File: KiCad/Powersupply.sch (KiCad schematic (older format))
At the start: 6 parts, among them J20 12V, U9 LM2596S-3.3

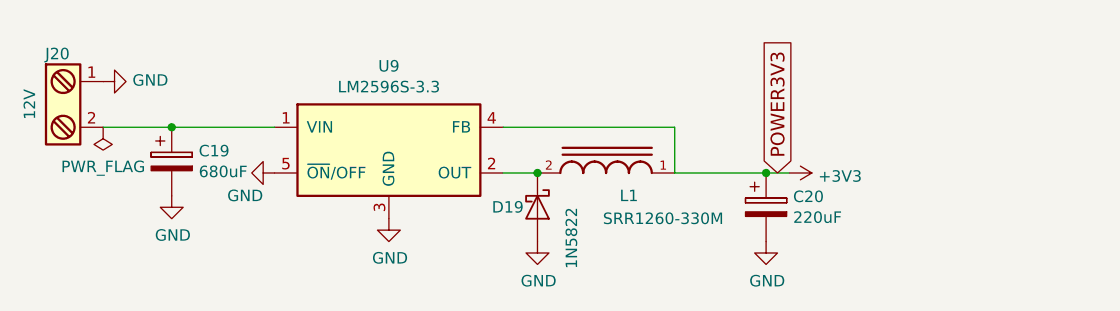
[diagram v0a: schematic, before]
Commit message: Use I2C for I/O
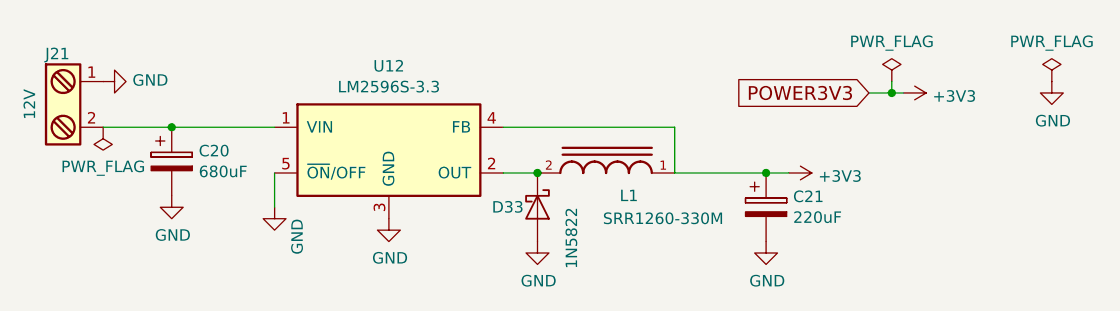
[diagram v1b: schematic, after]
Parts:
- L1: footprint INDP125125X600N -> SRR1260-330M:INDP125125X600N
- renumbered C19 to C20, C20 to C21, D19 to D33, J20 to J21, U9 to U12
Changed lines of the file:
@@
 LIBS:ESD_Protection
 LIBS:SRR1260-330M
+LIBS:ADS1115IDGST
 LIBS:HAP-IO-Card-cache
 EELAYER 26 0
@@
 $EndDescr
 $Comp
-L LM2596S-3.3 U9
+L LM2596S-3.3 U12
 U 1 1 591DBF8A
 P 2800 3600
-F 0 "U9" H 2800 3967 50  0000 C CNN
+F 0 "U12" H 2800 3967 50  0000 C CNN
 F 1 "LM2596S-3.3" H 2800 3876 50  0000 C CNN
 F 2 "TO_SOT_Packages_SMD:TO-263-5_TabPin3" H 3100 3350 50  0001 C CIN
@@
 $EndComp
 $Comp
-L GND #PWR034
+L GND #PWR069
 U 1 1 591DC03F
 P 2800 3900
-F 0 "#PWR034" H 2800 3650 50  0001 C CNN
+F 0 "#PWR069" H 2800 3650 50  0001 C CNN
 F 1 "GND" H 2805 3727 50  0000 C CNN
 F 2 "" H 2800 3900 50  0001 C CNN
@@
 $EndComp
 $Comp
-L +3V3 #PWR035
+L +3V3 #PWR070
 U 1 1 591DC078
 P 4550 3700
-F 0 "#PWR035" H 4550 3550 50  0001 C CNN
+F 0 "#PWR070" H 4550 3550 50  0001 C CNN
 F 1 "+3V3" V 4565 3828 50  0000 L CNN
 F 2 "" H 4550 3700 50  0001 C CNN
@@
 $EndComp
 $Comp
-L 1N5822 D19
+L 1N5822 D33
 U 1 1 591DD60B
 P 3450 3850
-F 0 "D19" V 3450 3650 50  0000 L CNN
+F 0 "D33" V 3450 3650 50  0000 L CNN
 F 1 "1N5822" H 3450 4000 50  0000 L CNN
 F 2 "Diodes_THT:D_5KPW_P7.62mm_Vertical_AnodeUp" H 3450 3675 50  0001 C CNN
@@
 Connection ~ 3450 3700
 $Comp
-L GND #PWR036
+L GND #PWR071
 U 1 1 591DD85A
 P 3450 4000
-F 0 "#PWR036" H 3450 3750 50  0001 C CNN
+F 0 "#PWR071" H 3450 3750 50  0001 C CNN
 F 1 "GND" H 3455 3827 50  0000 C CNN
 F 2 "" H 3450 4000 50  0001 C CNN
@@
 $EndComp
 $Comp
-L GND #PWR037
+L GND #PWR072
 U 1 1 591DD883
-P 2300 3700
-F 0 "#PWR037" H 2300 3450 50  0001 C CNN
-F 1 "GND" V 2400 3650 50  0000 R CNN
-F 2 "" H 2300 3700 50  0001 C CNN
-F 3 "" H 2300 3700 50  0001 C CNN
-	1    2300 3700
-	0    1    1    0
-$EndComp
-$Comp
-L Screw_Terminal_1x02 J20
+P 2300 3850
+F 0 "#PWR072" H 2300 3600 50  0001 C CNN
+F 1 "GND" V 2400 3800 50  0000 R CNN
+F 2 "" H 2300 3850 50  0001 C CNN
+F 3 "" H 2300 3850 50  0001 C CNN
+	1    2300 3850
+	1    0    0    -1
+$EndComp
+$Comp
+L Screw_Terminal_1x02 J21
 U 1 1 591DDB2C
 P 1350 3400
-F 0 "J20" H 1350 3650 50  0000 C TNN
+F 0 "J21" H 1350 3650 50  0000 C TNN
 F 1 "12V" V 1200 3400 50  0000 C TNN
 F 2 "Connectors_Terminal_Blocks:TerminalBlock_Pheonix_MPT-2.54mm_2pol" H 1350 3175 50  0001 C CNN
@@
 	1550 3500 2300 3500
 $Comp
-L GND #PWR038
+L GND #PWR073
 U 1 1 591DDBCC
 P 1550 3300
-F 0 "#PWR038" H 1550 3050 50  0001 C CNN
+F 0 "#PWR073" H 1550 3050 50  0001 C CNN
 F 1 "GND" V 1555 3172 50  0000 R CNN
 F 2 "" H 1550 3300 50  0001 C CNN
@@
 Wire Wire Line
 	4050 3700 4550 3700
-Text GLabel 4500 3700 1    60   Input ~ 0
+Text GLabel 4900 3350 0    60   Input ~ 0
 POWER3V3
 $Comp
-L PWR_FLAG #FLG039
+L PWR_FLAG #FLG074
 U 1 1 591E327D
 P 1550 3500
-F 0 "#FLG039" H 1550 3575 50  0001 C CNN
+F 0 "#FLG074" H 1550 3575 50  0001 C CNN
 F 1 "PWR_FLAG" H 1550 3673 50  0000 C CNN
 F 2 "" H 1550 3500 50  0001 C CNN
@@
 F 0 "L1" V 3650 3600 50  0000 C CNN
 F 1 "SRR1260-330M" V 3550 3450 50  0000 C CNN
-F 2 "INDP125125X600N" H 3750 3700 50  0001 L CNN
+F 2 "SRR1260-330M:INDP125125X600N" H 3750 3700 50  0001 L CNN
 F 3 "Inductor Power Shielded Wirewound 33uH 20%25 100KHz 27Q-Factor Ferrite 3A 60mOhm DCR T/R" H 3750 3700 50  0001 L CNN
 F 4 "Bad" H 3750 3700 50  0001 L CNN "Availability"
@@
 	4050 3500 3300 3500
 $Comp
-L CP C20
+L CP C21
 U 1 1 591E58F9
 P 4450 3850
-F 0 "C20" H 4568 3896 50  0000 L CNN
+F 0 "C21" H 4568 3896 50  0000 L CNN
 F 1 "220uF" H 4568 3805 50  0000 L CNN
 F 2 "Capacitors_THT:CP_Radial_D5.0mm_P2.00mm" H 4488 3700 50  0001 C CNN
@@
 $EndComp
 $Comp
-L GND #PWR040
+L GND #PWR075
 U 1 1 591E5956
 P 4450 4000
-F 0 "#PWR040" H 4450 3750 50  0001 C CNN
+F 0 "#PWR075" H 4450 3750 50  0001 C CNN
 F 1 "GND" H 4455 3827 50  0000 C CNN
 F 2 "" H 4450 4000 50  0001 C CNN
@@
 $EndComp
 $Comp
-L CP C19
+L CP C20
 U 1 1 591E59B2
 P 1850 3650
-F 0 "C19" H 1968 3696 50  0000 L CNN
+F 0 "C20" H 1968 3696 50  0000 L CNN
 F 1 "680uF" H 1968 3605 50  0000 L CNN
 F 2 "Capacitors_THT:CP_Radial_D8.0mm_P3.50mm" H 1888 3500 50  0001 C CNN
@@
 $EndComp
 $Comp
-L GND #PWR041
+L GND #PWR076
 U 1 1 591E5A32
 P 1850 3800
-F 0 "#PWR041" H 1850 3550 50  0001 C CNN
+F 0 "#PWR076" H 1850 3550 50  0001 C CNN
 F 1 "GND" H 1855 3627 50  0000 C CNN
 F 2 "" H 1850 3800 50  0001 C CNN
@@
 Connection ~ 4450 3700
 Connection ~ 1850 3500
+Wire Wire Line
+	2300 3850 2300 3700
+$Comp
+L +3V3 #PWR077
+U 1 1 592AD7CB
+P 5050 3350
+F 0 "#PWR077" H 5050 3200 50  0001 C CNN
+F 1 "+3V3" V 5065 3478 50  0000 L CNN
+F 2 "" H 5050 3350 50  0001 C CNN
+F 3 "" H 5050 3350 50  0001 C CNN
+	1    5050 3350
+	0    1    1    0
+$EndComp
+Wire Wire Line
+	5050 3350 4900 3350
+$Comp
+L PWR_FLAG #FLG078
+U 1 1 592B367C
+P 5000 3300
+F 0 "#FLG078" H 5000 3375 50  0001 C CNN
+F 1 "PWR_FLAG" H 5000 3474 50  0000 C CNN
+F 2 "" H 5000 3300 50  0001 C CNN
+F 3 "" H 5000 3300 50  0001 C CNN
+	1    5000 3300
+	1    0    0    -1
+$EndComp
+Wire Wire Line
+	5000 3300 5000 3350
+Connection ~ 5000 3350
+$Comp
+L PWR_FLAG #FLG079
+U 1 1 592B4E13
+P 5700 3300
+F 0 "#FLG079" H 5700 3375 50  0001 C CNN
+F 1 "PWR_FLAG" H 5700 3474 50  0000 C CNN
+F 2 "" H 5700 3300 50  0001 C CNN
+F 3 "" H 5700 3300 50  0001 C CNN
+	1    5700 3300
+	1    0    0    -1
+$EndComp
+$Comp
+L GND #PWR080
+U 1 1 592B4E96
+P 5700 3300
+F 0 "#PWR080" H 5700 3050 50  0001 C CNN
+F 1 "GND" H 5705 3127 50  0000 C CNN
+F 2 "" H 5700 3300 50  0001 C CNN
+F 3 "" H 5700 3300 50  0001 C CNN
+	1    5700 3300
+	1    0    0    -1
+$EndComp
 $EndSCHEMATC

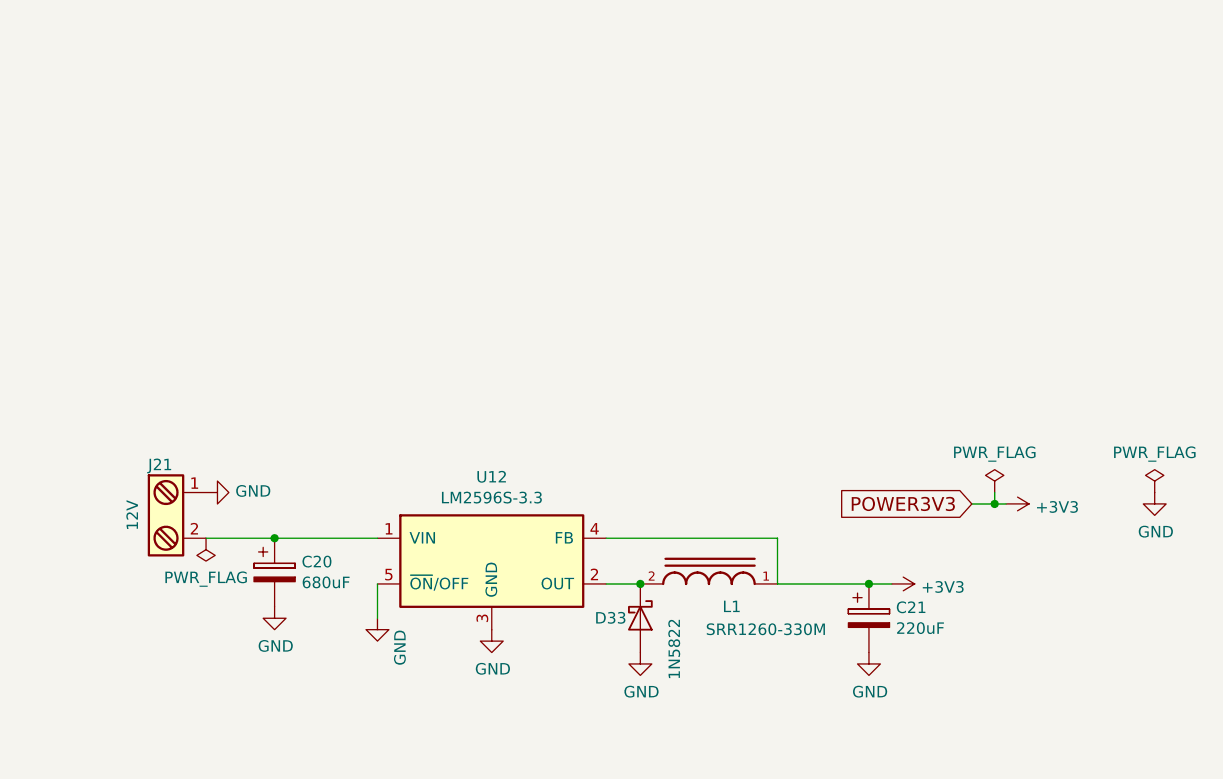
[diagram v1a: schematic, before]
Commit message: Reworked power-supply to provide 5V. Updated ESP-connections.
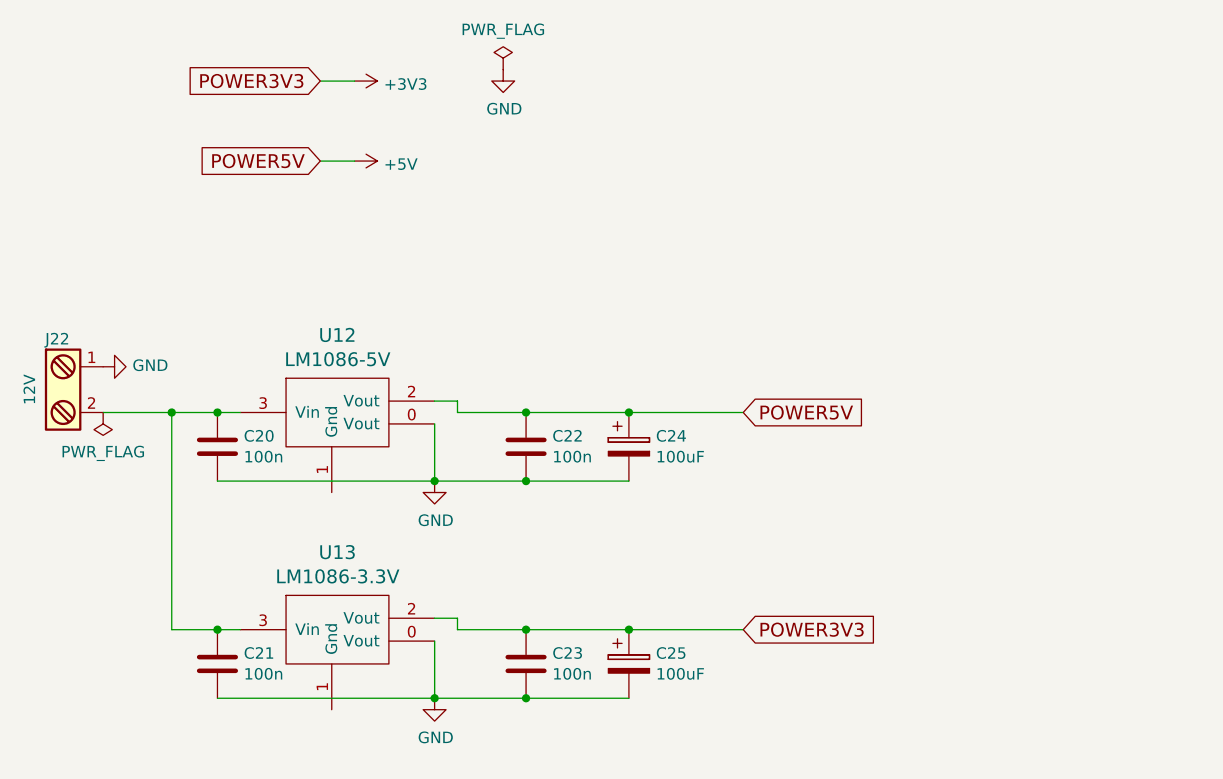
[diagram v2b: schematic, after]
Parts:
- removed C20: 680uF, Capacitors_THT:CP_Radial_D8.0mm_P3.50mm, symbol CP
- removed C21: 220uF, Capacitors_THT:CP_Radial_D5.0mm_P2.00mm, symbol CP
- removed D33: 1N5822, Diodes_THT:D_5KPW_P7.62mm_Vertical_AnodeUp, symbol 1N5822
- removed J21: 12V, Connectors_Terminal_Blocks:TerminalBlock_Pheonix_MPT-2.54mm_2pol, symbol Screw_Terminal_1x02
- removed L1: SRR1260-330M, SRR1260-330M:INDP125125X600N, symbol SRR1260-330M
- removed U12: LM2596S-3.3, TO_SOT_Packages_SMD:TO-263-5_TabPin3, symbol LM2596S-3.3
- added C20, C21, C22, C23: 100n, Capacitors_SMD:C_0805, symbol C
- added C24, C25: 100uF, Capacitors_THT:CP_Radial_D7.5mm_P2.50mm, symbol CP
- added J22: 12V, Connectors_Terminal_Blocks:TerminalBlock_Pheonix_MPT-2.54mm_2pol, symbol Screw_Terminal_1x02
- added U12: LM1086-5V, TO_SOT_Packages_THT:TO-220_Horizontal, symbol LM1086-5V
- added U13: LM1086-3.3V, TO_SOT_Packages_THT:TO-220_Horizontal, symbol LM1086-3.3V
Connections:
- net +3V3: now also C23.1, C25.1, U13.2 (Vout)
- net GND: now also C20.2, C21.2, C22.2, C23.2, C24.2, C25.2, J22.1, U12.0 (Vout), U13.0 (Vout)
- new net: C20.1, C21.1, J22.2, U12.3 (Vin), U13.3 (Vin)
- new net +5V: C22.1, C24.1, U12.2 (Vout)

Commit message: More work
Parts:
- removed U12: LM1086-5V, TO_SOT_Packages_THT:TO-220_Horizontal, symbol LM1086-5V
- removed U13: LM1086-3.3V, TO_SOT_Packages_THT:TO-220_Horizontal, symbol LM1086-3.3V
- added U501: LM1086-5V, TO_SOT_Packages_THT:TO-220_Horizontal, symbol LM1086-5V
- added U502: LM1086-3.3V, TO_SOT_Packages_THT:TO-220_Horizontal, symbol LM1086-3.3V
- renumbered C20 to C501, C21 to C502, C22 to C503, C23 to C504, C24 to C505, C25 to C506, J22 to J501
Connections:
- net +3V3: now also U502.0 (Vout), U502.2 (Vout)
- net +5V: now also U501.0 (Vout), U501.2 (Vout)
- net GND: now also U501.1 (Gnd), U502.1 (Gnd)
- net Input12V: now reaches C501.1, C502.1, J501.2
- net Input12V: now also U501.3 (Vin), U502.3 (Vin)
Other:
- note added: "Max 1.5A"
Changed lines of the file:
@@
 EESchema Schematic File Version 2
-LIBS:HAP-IO-Card-rescue
 LIBS:power
 LIBS:device
@@
 $EndComp
 Wire Wire Line
-	2050 1500 2200 1500
+	2100 1500 2200 1500
 $Comp
 L PWR_FLAG #FLG073
@@
 $EndComp
 $Comp
-L LM1086-5V U12
-U 1 1 5924BD40
-P 2150 2550
-F 0 "U12" H 2125 2487 60  0000 C CNN
-F 1 "LM1086-5V" H 2125 2381 60  0000 C CNN
-F 2 "TO_SOT_Packages_THT:TO-220_Horizontal" H 2150 2550 60  0001 C CNN
-F 3 "http://se.rs-online.com/web/p/low-dropout-voltage-regulators/5358578/" H 2150 2550 60  0001 C CNN
-	1    2150 2550
-	1    0    0    -1
-$EndComp
-$Comp
-L LM1086-3.3V U13
-U 1 1 5924BDCF
-P 2150 3500
-F 0 "U13" H 2125 3437 60  0000 C CNN
-F 1 "LM1086-3.3V" H 2125 3331 60  0000 C CNN
-F 2 "TO_SOT_Packages_THT:TO-220_Horizontal" H 2150 3500 60  0001 C CNN
-F 3 "" H 2150 3500 60  0001 C CNN
-	1    2150 3500
-	1    0    0    -1
-$EndComp
-$Comp
 L GND #PWR075
 U 1 1 5924C039
-P 2550 4200
-F 0 "#PWR075" H 2550 3950 50  0001 C CNN
-F 1 "GND" H 2555 4027 50  0000 C CNN
-F 2 "" H 2550 4200 50  0001 C CNN
-F 3 "" H 2550 4200 50  0001 C CNN
-	1    2550 4200
-	1    0    0    -1
-$EndComp
-$Comp
-L C C21
+P 2550 4250
+F 0 "#PWR075" H 2550 4000 50  0001 C CNN
+F 1 "GND" H 2555 4077 50  0000 C CNN
+F 2 "" H 2550 4250 50  0001 C CNN
+F 3 "" H 2550 4250 50  0001 C CNN
+	1    2550 4250
+	1    0    0    -1
+$EndComp
+$Comp
+L C C502
 U 1 1 5924C072
 P 1600 4050
-F 0 "C21" H 1715 4096 50  0000 L CNN
+F 0 "C502" H 1715 4096 50  0000 L CNN
 F 1 "100n" H 1715 4005 50  0000 L CNN
 F 2 "Capacitors_SMD:C_0805" H 1638 3900 50  0001 C CNN
@@
 $EndComp
 $Comp
-L C C23
+L C C504
 U 1 1 5924C361
 P 2950 4050
-F 0 "C23" H 3065 4096 50  0000 L CNN
+F 0 "C504" H 3065 4096 50  0000 L CNN
 F 1 "100n" H 3065 4005 50  0000 L CNN
 F 2 "Capacitors_SMD:C_0805" H 2988 3900 50  0001 C CNN
@@
 $EndComp
 $Comp
-L CP C25
+L CP C506
 U 1 1 5924C4E4
 P 3400 4050
-F 0 "C25" H 3518 4096 50  0000 L CNN
+F 0 "C506" H 3518 4096 50  0000 L CNN
 F 1 "100uF" H 3518 4005 50  0000 L CNN
 F 2 "Capacitors_THT:CP_Radial_D7.5mm_P2.50mm" H 3438 3900 50  0001 C CNN
@@
 $EndComp
 Wire Wire Line
-	2550 3950 2550 4200
-Wire Wire Line
-	1600 4200 3400 4200
-Connection ~ 2550 4200
-Connection ~ 2950 4200
-Wire Wire Line
 	2650 3900 3900 3900
 Wire Wire Line
-	2650 3900 2650 3850
+	2650 3850 2650 3950
 Wire Wire Line
 	2650 3850 2550 3850
@@
 Connection ~ 1600 3900
 $Comp
-L GND #PWR076
-U 1 1 5924DE5E
-P 2550 3250
-F 0 "#PWR076" H 2550 3000 50  0001 C CNN
-F 1 "GND" H 2555 3077 50  0000 C CNN
-F 2 "" H 2550 3250 50  0001 C CNN
-F 3 "" H 2550 3250 50  0001 C CNN
-	1    2550 3250
-	1    0    0    -1
-$EndComp
-$Comp
-L C C20
+L C C501
 U 1 1 5924DE64
 P 1600 3100
-F 0 "C20" H 1715 3146 50  0000 L CNN
+F 0 "C501" H 1715 3146 50  0000 L CNN
 F 1 "100n" H 1715 3055 50  0000 L CNN
 F 2 "Capacitors_SMD:C_0805" H 1638 2950 50  0001 C CNN
@@
 	1    0    0    -1
 $EndComp
-$Comp
-L C C22
-U 1 1 5924DE6A
-P 2950 3100
-F 0 "C22" H 3065 3146 50  0000 L CNN
-F 1 "100n" H 3065 3055 50  0000 L CNN
-F 2 "Capacitors_SMD:C_0805" H 2988 2950 50  0001 C CNN
-F 3 "" H 2950 3100 50  0001 C CNN
-	1    2950 3100
-	1    0    0    -1
-$EndComp
-Wire Wire Line
-	2550 3000 2550 3250
-Wire Wire Line
-	1600 3250 3400 3250
-Connection ~ 2550 3250
-Connection ~ 2950 3250
 Wire Wire Line
 	2650 2950 3900 2950
-Wire Wire Line
-	2650 2950 2650 2900
 Wire Wire Line
 	2650 2900 2550 2900
@@
 	1100 2950 1700 2950
 $Comp
-L GND #PWR077
+L GND #PWR076
 U 1 1 5924DE85
-P 1100 2750
-F 0 "#PWR077" H 1100 2500 50  0001 C CNN
-F 1 "GND" V 1105 2622 50  0000 R CNN
-F 2 "" H 1100 2750 50  0001 C CNN
-F 3 "" H 1100 2750 50  0001 C CNN
-	1    1100 2750
+P 1350 2750
+F 0 "#PWR076" H 1350 2500 50  0001 C CNN
+F 1 "GND" V 1355 2622 50  0000 R CNN
+F 2 "" H 1350 2750 50  0001 C CNN
+F 3 "" H 1350 2750 50  0001 C CNN
+	1    1350 2750
 	0    -1   -1   0
 $EndComp
 $Comp
-L PWR_FLAG #FLG078
+L PWR_FLAG #FLG077
 U 1 1 5924DE8B
 P 1100 2950
-F 0 "#FLG078" H 1100 3025 50  0001 C CNN
+F 0 "#FLG077" H 1100 3025 50  0001 C CNN
 F 1 "PWR_FLAG" H 1100 3123 50  0000 C CNN
 F 2 "" H 1100 2950 50  0001 C CNN
@@
 Connection ~ 1600 2950
 $Comp
-L Screw_Terminal_1x02 J22
+L Screw_Terminal_1x02 J501
 U 1 1 5924DE7F
 P 900 2850
-F 0 "J22" H 900 3100 50  0000 C TNN
+F 0 "J501" H 900 3100 50  0000 C TNN
 F 1 "12V" V 750 2850 50  0000 C TNN
 F 2 "Connectors_Terminal_Blocks:TerminalBlock_Pheonix_MPT-2.54mm_2pol" H 900 2625 50  0001 C CNN
@@
 POWER5V
 Connection ~ 3400 2950
-Text GLabel 2050 1500 0    60   Input ~ 0
+Text GLabel 2100 1500 0    60   Input ~ 0
 POWER3V3
 Text GLabel 2050 1850 0    60   Input ~ 0
@@
 	2050 1850 2200 1850
 $Comp
-L +5V #PWR079
+L +5V #PWR078
 U 1 1 5924EF19
 P 2200 1850
-F 0 "#PWR079" H 2200 1700 50  0001 C CNN
+F 0 "#PWR078" H 2200 1700 50  0001 C CNN
 F 1 "+5V" V 2215 1978 50  0000 L CNN
 F 2 "" H 2200 1850 50  0001 C CNN
@@
 $EndComp
 $Comp
-L CP C24
+L CP C505
 U 1 1 5924F50A
 P 3400 3100
-F 0 "C24" H 3518 3146 50  0000 L CNN
+F 0 "C505" H 3518 3146 50  0000 L CNN
 F 1 "100uF" H 3518 3055 50  0000 L CNN
 F 2 "Capacitors_THT:CP_Radial_D7.5mm_P2.50mm" H 3438 2950 50  0001 C CNN
@@
 	1    0    0    -1
 $EndComp
+Text Notes 3950 3100 0    60   ~ 0
+Max 1.5A
+Text Notes 4000 4050 0    60   ~ 0
+Max 1.5A
+Text Label 1300 2950 0    60   ~ 0
+Input12V
+Text Label 2200 1500 0    60   ~ 0
+3V3
+Text Label 2200 1850 0    60   ~ 0
+5V
+Connection ~ 2650 2950
+$Comp
+L C C503
+U 1 1 5924DE6A
+P 2950 3100
+F 0 "C503" H 3065 3146 50  0000 L CNN
+F 1 "100n" H 3065 3055 50  0000 L CNN
+F 2 "Capacitors_SMD:C_0805" H 2988 2950 50  0001 C CNN
+F 3 "" H 2950 3100 50  0001 C CNN
+	1    2950 3100
+	1    0    0    -1
+$EndComp
+$Comp
+L GND #PWR079
+U 1 1 5924DE5E
+P 2550 3300
+F 0 "#PWR079" H 2550 3050 50  0001 C CNN
+F 1 "GND" H 2555 3127 50  0000 C CNN
+F 2 "" H 2550 3300 50  0001 C CNN
+F 3 "" H 2550 3300 50  0001 C CNN
+	1    2550 3300
+	1    0    0    -1
+$EndComp
+Wire Wire Line
+	1600 3300 3400 3300
+Wire Wire Line
+	1600 3300 1600 3250
+Connection ~ 2100 3300
+Wire Wire Line
+	3400 3300 3400 3250
+Wire Wire Line
+	2950 3300 2950 3250
+Connection ~ 2550 3300
+Connection ~ 2950 3300
+Wire Wire Line
+	2650 3000 2550 3000
+Wire Wire Line
+	2650 2900 2650 3000
+Wire Wire Line
+	1600 4200 1600 4250
+Wire Wire Line
+	1600 4250 3400 4250
+Connection ~ 2100 4250
+Wire Wire Line
+	2950 4250 2950 4200
+Connection ~ 2550 4250
+Wire Wire Line
+	3400 4250 3400 4200
+Connection ~ 2950 4250
+Wire Wire Line
+	2650 3950 2550 3950
+Connection ~ 2650 3900
+$Comp
+L LM1086-3.3V U502
+U 1 1 59269042
+P 2150 3500
+F 0 "U502" H 2125 3437 60  0000 C CNN
+F 1 "LM1086-3.3V" H 2125 3331 60  0000 C CNN
+F 2 "TO_SOT_Packages_THT:TO-220_Horizontal" H 2150 3500 60  0001 C CNN
+F 3 "" H 2150 3500 60  0001 C CNN
+	1    2150 3500
+	1    0    0    -1
+$EndComp
+$Comp
+L LM1086-5V U501
+U 1 1 592690D5
+P 2150 2550
+F 0 "U501" H 2125 2487 60  0000 C CNN
+F 1 "LM1086-5V" H 2125 2381 60  0000 C CNN
+F 2 "TO_SOT_Packages_THT:TO-220_Horizontal" H 2150 2550 60  0001 C CNN
+F 3 "" H 2150 2550 60  0001 C CNN
+	1    2150 2550
+	1    0    0    -1
+$EndComp
+Wire Wire Line
+	1100 2750 1350 2750
+Text Label 1150 2750 0    60   ~ 0
+12VGND
 $EndSCHEMATC
